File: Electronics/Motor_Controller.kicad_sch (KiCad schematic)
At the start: 4 parts, among them U1 RP2040, U4 W25Q32JVZP

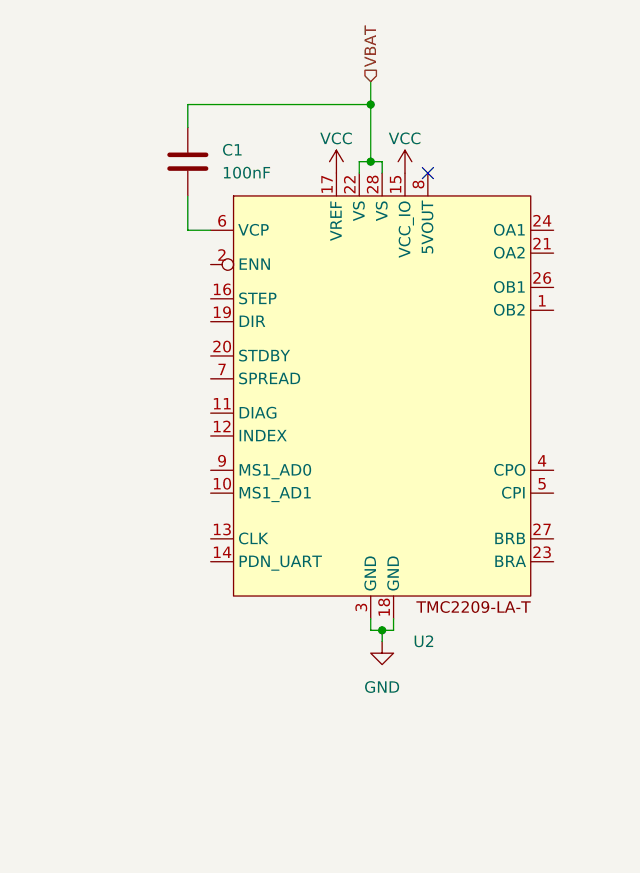
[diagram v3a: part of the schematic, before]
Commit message: update gitignore
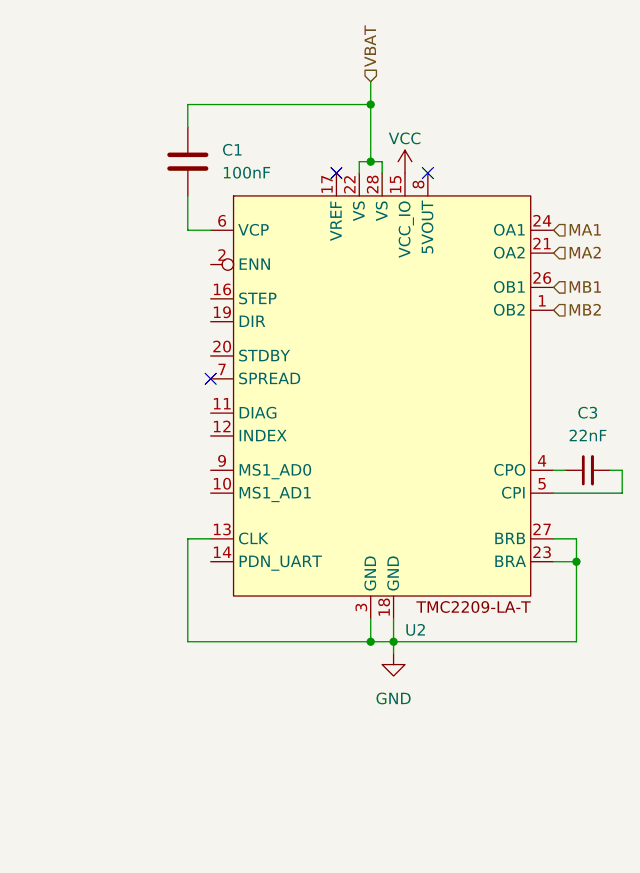
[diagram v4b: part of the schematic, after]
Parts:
- added C3: 22nF, symbol Device:C_Small
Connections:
- net GND: now also U2.13 (CLK), U2.23 (BRA), U2.27 (BRB)
- net VCC: no longer U2.17 (VREF)
- net MB2: now reaches U2.1 (OB2)
- net MA2: now reaches U2.21 (OA2)
- net MA1: now reaches U2.24 (OA1)
- net MB1: now reaches U2.26 (OB1)
- net at U2.4 (CPO): now also C3.1
- net at U2.5 (CPI): now also C3.2
- no-connect marks 1 -> 3
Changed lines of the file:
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@@
 (kicad_sch (version 20230121) (generator eeschema)
   (paper "A4")
+  (junction (at 196.85 87.63) (diameter 0) (color 0 0 0 0)
+  )
+  (junction (at 217.17 78.74) (diameter 0) (color 0 0 0 0)
+  )
   (junction (at 194.31 27.94) (diameter 0) (color 0 0 0 0)
   )
   (junction (at 194.31 34.29) (diameter 0) (color 0 0 0 0)
   )
-  (junction (at 195.58 86.36) (diameter 0) (color 0 0 0 0)
-  )
+  (junction (at 194.31 87.63) (diameter 0) (color 0 0 0 0)
+  )
+  (no_connect (at 190.5 35.56))
+  (no_connect (at 176.53 58.42))
   (no_connect (at 200.66 35.56))
   (wire (pts (xy 194.31 34.29) (xy 195.58 34.29))
     (stroke (width 0) (type default))
   )
+  (wire (pts (xy 214.63 68.58) (xy 215.9 68.58))
+    (stroke (width 0) (type default))
+  )
   (wire (pts (xy 194.31 25.4) (xy 194.31 27.94))
     (stroke (width 0) (type default))
   )
+  (wire (pts (xy 196.85 87.63) (xy 217.17 87.63))
+    (stroke (width 0) (type default))
+  )
   (wire (pts (xy 173.99 27.94) (xy 194.31 27.94))
     (stroke (width 0) (type default))
@@
     (stroke (width 0) (type default))
   )
-  (wire (pts (xy 194.31 85.09) (xy 194.31 86.36))
+  (wire (pts (xy 194.31 85.09) (xy 194.31 87.63))
+    (stroke (width 0) (type default))
+  )
+  (wire (pts (xy 222.25 71.12) (xy 214.63 71.12))
     (stroke (width 0) (type default))
   )
@@
     (stroke (width 0) (type default))
   )
+  (wire (pts (xy 217.17 87.63) (xy 217.17 78.74))
+    (stroke (width 0) (type default))
+  )
   (wire (pts (xy 173.99 41.91) (xy 173.99 38.1))
     (stroke (width 0) (type default))
   )
+  (wire (pts (xy 217.17 78.74) (xy 214.63 78.74))
+    (stroke (width 0) (type default))
+  )
   (wire (pts (xy 193.04 34.29) (xy 193.04 35.56))
     (stroke (width 0) (type default))
   )
+  (wire (pts (xy 217.17 76.2) (xy 217.17 78.74))
+    (stroke (width 0) (type default))
+  )
   (wire (pts (xy 194.31 27.94) (xy 194.31 34.29))
     (stroke (width 0) (type default))
   )
-  (wire (pts (xy 194.31 86.36) (xy 195.58 86.36))
-    (stroke (width 0) (type default))
-  )
-  (wire (pts (xy 195.58 86.36) (xy 196.85 86.36))
-    (stroke (width 0) (type default))
-  )
-  (wire (pts (xy 195.58 86.36) (xy 195.58 87.63))
-    (stroke (width 0) (type default))
-  )
-  (wire (pts (xy 196.85 85.09) (xy 196.85 86.36))
-    (stroke (width 0) (type default))
+  (wire (pts (xy 194.31 87.63) (xy 196.85 87.63))
+    (stroke (width 0) (type default))
+  )
+  (wire (pts (xy 173.99 87.63) (xy 194.31 87.63))
+    (stroke (width 0) (type default))
+  )
+  (wire (pts (xy 214.63 76.2) (xy 217.17 76.2))
+    (stroke (width 0) (type default))
+  )
+  (wire (pts (xy 173.99 76.2) (xy 173.99 87.63))
+    (stroke (width 0) (type default))
+  )
+  (wire (pts (xy 196.85 88.9) (xy 196.85 87.63))
+    (stroke (width 0) (type default))
+  )
+  (wire (pts (xy 222.25 68.58) (xy 222.25 71.12))
+    (stroke (width 0) (type default))
+  )
+  (wire (pts (xy 196.85 85.09) (xy 196.85 87.63))
+    (stroke (width 0) (type default))
+  )
+  (wire (pts (xy 176.53 76.2) (xy 173.99 76.2))
+    (stroke (width 0) (type default))
+  )
+  (wire (pts (xy 220.98 68.58) (xy 222.25 68.58))
+    (stroke (width 0) (type default))
+  )
+  (hierarchical_label "MB2" (shape input) (at 214.63 50.8 0) (fields_autoplaced)
+    (effects (font (size 1.27 1.27)) (justify left))
+  )
+  (hierarchical_label "MA2" (shape input) (at 214.63 44.45 0) (fields_autoplaced)
+    (effects (font (size 1.27 1.27)) (justify left))
+  )
+  (hierarchical_label "MA1" (shape input) (at 214.63 41.91 0) (fields_autoplaced)
+    (effects (font (size 1.27 1.27)) (justify left))
   )
   (hierarchical_label "VBAT" (shape input) (at 194.31 25.4 90) (fields_autoplaced)
     (effects (font (size 1.27 1.27)) (justify left))
   )
+  (hierarchical_label "MB1" (shape input) (at 214.63 48.26 0) (fields_autoplaced)
+    (effects (font (size 1.27 1.27)) (justify left))
+  )
   (symbol (lib_id "TMC2209-LA-T:TMC2209-LA-T") (at 195.58 60.96 0) (unit 1)
-    (in_bom yes) (on_board yes) (dnp no) (fields_autoplaced)
-    (property "Reference" "U2" (at 199.0441 87.63 0)
+    (in_bom yes) (on_board yes) (dnp no)
+    (property "Reference" "U2" (at 198.12 86.36 0)
       (effects (font (size 1.27 1.27)) (justify left))
     )
@@
         (path "/4c70cac4-2e87-4919-a1c8-fe5f41acf493/95aef9fc-3811-4af8-99a5-cda59dbef7fc"
           (reference "U2") (unit 1)
-        )
-      )
-    )
-  )
-  (symbol (lib_id "power:VCC") (at 190.5 35.56 0) (unit 1)
-    (in_bom yes) (on_board yes) (dnp no)
-    (property "Reference" "#PWR06" (at 190.5 39.37 0)
-      (effects (font (size 1.27 1.27)) hide)
-    )
-    (property "Value" "VCC" (at 190.5 31.75 0)
-      (effects (font (size 1.27 1.27)))
-    )
-    (property "Footprint" "" (at 190.5 35.56 0)
-      (effects (font (size 1.27 1.27)) hide)
-    )
-    (property "Datasheet" "" (at 190.5 35.56 0)
-      (effects (font (size 1.27 1.27)) hide)
-    )
-    (pin "1")
-    (instances
-      (project "Electronics"
-        (path "/4c70cac4-2e87-4919-a1c8-fe5f41acf493/95aef9fc-3811-4af8-99a5-cda59dbef7fc"
-          (reference "#PWR06") (unit 1)
         )
       )
@@
     )
   )
+  (symbol (lib_id "Device:C_Small") (at 218.44 68.58 90) (unit 1)
+    (in_bom yes) (on_board yes) (dnp no)
+    (property "Reference" "C3" (at 218.4463 62.23 90)
+      (effects (font (size 1.27 1.27)))
+    )
+    (property "Value" "22nF" (at 218.44 64.77 90)
+      (effects (font (size 1.27 1.27)))
+    )
+    (property "Footprint" "" (at 218.44 68.58 0)
+      (effects (font (size 1.27 1.27)) hide)
+    )
+    (property "Datasheet" "~" (at 218.44 68.58 0)
+      (effects (font (size 1.27 1.27)) hide)
+    )
+    (pin "1")
+    (pin "2")
+    (instances
+      (project "Electronics"
+        (path "/4c70cac4-2e87-4919-a1c8-fe5f41acf493/95aef9fc-3811-4af8-99a5-cda59dbef7fc"
+          (reference "C3") (unit 1)
+        )
+      )
+    )
+  )
   (symbol (lib_id "Device:C") (at 173.99 34.29 0) (unit 1)
     (in_bom yes) (on_board yes) (dnp no)
@@
     )
   )
-  (symbol (lib_id "power:GND") (at 195.58 87.63 0) (unit 1)
+  (symbol (lib_id "power:GND") (at 196.85 88.9 0) (unit 1)
     (in_bom yes) (on_board yes) (dnp no) (fields_autoplaced)
-    (property "Reference" "#PWR08" (at 195.58 93.98 0)
-      (effects (font (size 1.27 1.27)) hide)
-    )
-    (property "Value" "GND" (at 195.58 92.71 0)
-      (effects (font (size 1.27 1.27)))
-    )
-    (property "Footprint" "" (at 195.58 87.63 0)
-      (effects (font (size 1.27 1.27)) hide)
-    )
-    (property "Datasheet" "" (at 195.58 87.63 0)
-      (effects (font (size 1.27 1.27)) hide)
-    )
+    (property "Reference" "#PWR08" (at 196.85 95.25 0)
+      (effects (font (size 1.27 1.27)) hide)
+    )
+    (property "Value" "GND" (at 196.85 93.98 0)
+      (effects (font (size 1.27 1.27)))
+    )
+    (property "Footprint" "" (at 196.85 88.9 0)
+      (effects (font (size 1.27 1.27)) hide)
+    )
+    (property "Datasheet" "" (at 196.85 88.9 0)
+      (effects (font (size 1.27 1.27)) hide)
+    )

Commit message: motor driver finished!
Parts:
- added C10, C11, C12, C13, C14, C17, C18, C22, C5, C7, C8, C9: 100nF, symbol Device:C
- added C15, C16, C4: 1uF, symbol Device:C
- added C19, C20: 15pF, symbol Device:C
- added C21: 10uF, symbol Device:C
- added C6: 22nF, symbol Device:C_Small
- added D2: ML_LED, symbol Device:LED
- added D3: MR_LED, symbol Device:LED
- added D4: RP2040_LED, symbol Device:LED
- added J2: SWCLK SWD, symbol Connector:Conn_01x02_Pin
- added R10, R9: 27.4, symbol Device:R
- added R11, R12, R4, R5, R6, R7, R8: 1k, symbol Device:R
- added R2: 22k, symbol Device:R
- added R3: 10k, symbol Device:R
- added SW1: SW_Push, symbol Switch:SW_Push
- added SW2: ~{USB_BOOT}, symbol Switch:SW_SPST
- added U6: ~, Package_DFN_QFN:QFN-28-1EP_5x5mm_P0.5mm_EP3.75x3.75mm, symbol TMC2209-LA-T:TMC2209-LA-T
- added Y1: ABM8-272-T3, symbol Device:Crystal_GND24
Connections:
- net GND: now also U1.19 (TESTEN), U1.57 (GND), U2.20 (STDBY), U4.4 (GND), U4.9 (EP), C10.2, C11.2, C12.2, C13.2, C14.2, C15.2, C16.2, C17.2, C18.2, C19.1, C20.1, C21.2, C22.2, C4.2, C7.2, C8.2, C9.2, D2.1 (K), D3.1 (K), D4.1 (K), SW1.1, SW2.2 (B), U6.13 (CLK), U6.18 (GND), U6.20 (STDBY), U6.23 (BRA), U6.27 (BRB), U6.3 (GND), Y1.2, Y1.4
- net VBAT: now also C5.1, U6.22 (VS), U6.28 (VS)
- net VCC: now also U1.1 (IOVDD), U1.10 (IOVDD), U1.22 (IOVDD), U1.33 (IOVDD), U1.42 (IOVDD), U1.43 (ADC_AVDD), U1.44 (VREG_IN), U1.48 (USB_VDD), U1.49 (IOVDD), U4.8 (VCC), C10.1, C11.1, C12.1, C13.1, C14.1, C15.1, C21.1, C7.1, C8.1, C9.1, R11.1, R3.1, U6.15 (VCC_IO)
- net ML_DIAG: now reaches U2.11 (DIAG)
- net ML_DIAG: now also U1.16 (GPIO13)
- net ML_INDEX: now reaches U2.12 (INDEX)
- net ML_INDEX: now also U1.17 (GPIO14)
- net ML_UART: now reaches U2.14 (PDN_UART)
- net ML_UART: now also U1.3 (GPIO1), R6.2
- net ML_STEP: now reaches U2.16 (STEP)
- net ML_STEP: now also U1.13 (GPIO10)
- net CURR_S: now reaches U2.17 (VREF)
- net CURR_S: now also U1.11 (GPIO8), C4.1, R2.2, U6.17 (VREF)
- net ML_DIR: now reaches U2.19 (DIR)
- net ML_DIR: now also U1.14 (GPIO11)
- net ~{ML_EN}: now reaches U2.2 (ENN)
- net ~{ML_EN}: now also U1.12 (GPIO9)
- net ML_SPRD: now reaches U2.7 (SPREAD)
- net ML_SPRD: now also U1.15 (GPIO12)
- net at U2.8 (5VOUT): now also R4.1
- net ~{MR_EN}: now reaches U1.18 (GPIO15)
- net ~{MR_EN}: now also U6.2 (ENN)
- net at U1.2 (GPIO0): now also R6.1
- net at U1.20 (XIN): now also C19.2, Y1.1
- net at U1.21 (XOUT): now also C20.2, Y1.3
- net at U1.23 (DVDD), U1.50 (DVDD): now also U1.45 (VREG_VOUT), C16.1, C17.1, C18.1
- net at U1.24 (SWCLK): now also J2.1 (Pin_1)
- net at U1.25 (SWD): now also J2.2 (Pin_2)
- net at U1.26 (RUN): now also C22.1, R11.2, SW1.2
- net MR_STEP: now reaches U1.27 (GPIO16)
- net MR_STEP: now also U6.16 (STEP)
- net MR_DIR: now reaches U1.28 (GPIO17)
- net MR_DIR: now also U6.19 (DIR)
- net MR_SPRD: now reaches U1.29 (GPIO18)
- net MR_SPRD: now also U6.7 (SPREAD)
- net MR_DIAG: now reaches U1.30 (GPIO19)
- net MR_DIAG: now also U6.11 (DIAG)
- net MR_INDEX: now reaches U1.31 (GPIO20)
- net MR_INDEX: now also U6.12 (INDEX)
- net at U1.32 (GPIO21): now also R8.1
- net SDA: now reaches U1.34 (GPIO22)
- net SCL: now reaches U1.35 (GPIO23)
- net at U1.37 (GPIO25): now also R2.1
- net at U1.46 (USB_DM): now also R10.2
- net at U1.47 (USB_DP): now also R9.2
- net QSPI_SD3: now reaches U1.51 (QSPI_SD3)
- net QSPI_SD3: now also U4.7 (IO3)
- net QSPI_SCLK: now reaches U1.52 (QSPI_SCLK)
- net QSPI_SCLK: now also U4.6 (CLK)
- net QSPI_SD0: now reaches U1.53 (QSPI_SD0)
- net QSPI_SD0: now also U4.5 (DI(IO0))
- net QSPI_SD2: now reaches U1.54 (QSPI_SD2)
- net QSPI_SD2: now also U4.3 (IO2)
- net QSPI_SD1: now reaches U1.55 (QSPI_SD1)
- net QSPI_SD1: now also U4.2 (DO(IO1))
- net QSPI_SS: now reaches U1.56 (QSPI_SS)
- net QSPI_SS: now also U4.1 (~{CS}), R12.1, R3.2
- net at U1.6 (GPIO4): now also R7.1
- net MR_UART: now reaches U1.7 (GPIO5)
- net MR_UART: now also R7.2, U6.14 (PDN_UART)
- net MA1 renamed ML_A1
- net MA2 renamed ML_A2
- net MB1 renamed ML_B1
- net MB2 renamed ML_B2
- new net: C6.1, U6.4 (CPO)
- new net: C6.2, U6.5 (CPI)
- new net: C5.2, U6.6 (VCP)
- new net: R5.1, U6.8 (5VOUT)
- new net: R12.2, SW2.1 (A)
- new net: D2.2 (A), R4.2
- new net: D3.2 (A), R5.2
- new net: D4.2 (A), R8.2
- new net MR_A1: U6.24 (OA1)
- new net MR_A2: U6.21 (OA2)
- new net MR_B1: U6.26 (OB1)
- new net MR_B2: U6.1 (OB2)
- new net USB+: R9.1
- new net USB-: R10.1
- no-connect marks 3 -> 13
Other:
- note added: "FLASH MEMORY"
- note added: "MCU"
- note added: "MOTOR DRIVERS"
- note added: "POWER"
- moved on the sheet: C1, C3, U1, U2, U4

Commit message: gyros done
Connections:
- net READY: now reaches U1.36 (GPIO24)
- no-connect marks 13 -> 12
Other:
- moved on the sheet: C4, R2
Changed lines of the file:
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@@
   (junction (at 160.02 121.92) (diameter 0) (color 0 0 0 0)
   )
-  (junction (at 118.11 105.41) (diameter 0) (color 0 0 0 0)
+  (junction (at 121.92 105.41) (diameter 0) (color 0 0 0 0)
   )
   (junction (at 182.88 121.92) (diameter 0) (color 0 0 0 0)
@@
   (junction (at 203.2 86.36) (diameter 0) (color 0 0 0 0)
   )
+  (junction (at 121.92 128.27) (diameter 0) (color 0 0 0 0)
+  )
   (junction (at 38.1 87.63) (diameter 0) (color 0 0 0 0)
   )
@@
   )
   (junction (at 44.45 179.07) (diameter 0) (color 0 0 0 0)
-  )
-  (junction (at 118.11 128.27) (diameter 0) (color 0 0 0 0)
   )
   (junction (at 19.05 97.79) (diameter 0) (color 0 0 0 0)
@@
   (no_connect (at 162.56 67.31))
   (no_connect (at 106.68 115.57))
-  (no_connect (at 106.68 102.87))
   (no_connect (at 106.68 59.69))
   (no_connect (at 229.87 69.85))
@@
     (stroke (width 0) (type default))
   )
-  (wire (pts (xy 116.84 105.41) (xy 118.11 105.41))
+  (wire (pts (xy 120.65 105.41) (xy 121.92 105.41))
     (stroke (width 0) (type default))
   )
@@
     (stroke (width 0) (type default))
   )
-  (wire (pts (xy 118.11 105.41) (xy 118.11 109.22))
-    (stroke (width 0) (type default))
-  )
-  (wire (pts (xy 118.11 128.27) (xy 134.62 128.27))
+  (wire (pts (xy 121.92 105.41) (xy 121.92 109.22))
     (stroke (width 0) (type default))
   )
@@
     (stroke (width 0) (type default))
   )
-  (wire (pts (xy 118.11 128.27) (xy 118.11 116.84))
+  (wire (pts (xy 121.92 128.27) (xy 121.92 116.84))
     (stroke (width 0) (type default))
   )
@@
     (stroke (width 0) (type default))
   )
-  (wire (pts (xy 81.28 128.27) (xy 118.11 128.27))
+  (wire (pts (xy 81.28 128.27) (xy 121.92 128.27))
     (stroke (width 0) (type default))
   )
@@
     (stroke (width 0) (type default))
   )
-  (wire (pts (xy 106.68 105.41) (xy 109.22 105.41))
+  (wire (pts (xy 106.68 105.41) (xy 113.03 105.41))
     (stroke (width 0) (type default))
   )
@@
     (stroke (width 0) (type default))
   )
+  (wire (pts (xy 121.92 128.27) (xy 134.62 128.27))
+    (stroke (width 0) (type default))
+  )
   (wire (pts (xy 119.38 22.86) (xy 119.38 24.13))
     (stroke (width 0) (type default))
@@
     (stroke (width 0) (type default))
   )
-  (wire (pts (xy 118.11 105.41) (xy 127 105.41))
+  (wire (pts (xy 121.92 105.41) (xy 130.81 105.41))
     (stroke (width 0) (type default))
   )
@@
     (effects (font (size 1.27 1.27)) (justify right bottom))
   )
-  (label "CURR_S" (at 127 105.41 180) (fields_autoplaced)
+  (label "CURR_S" (at 130.81 105.41 180) (fields_autoplaced)
     (effects (font (size 1.27 1.27)) (justify right bottom))
   )
@@
   )
   (hierarchical_label "MR_B1" (shape output) (at 267.97 46.99 0) (fields_autoplaced)
+    (effects (font (size 1.27 1.27)) (justify left))
+  )
+  (hierarchical_label "READY" (shape output) (at 106.68 102.87 0) (fields_autoplaced)
     (effects (font (size 1.27 1.27)) (justify left))
   )
@@
     )
   )
-  (symbol (lib_id "Device:R") (at 113.03 105.41 90) (unit 1)
-    (in_bom yes) (on_board yes) (dnp no)
-    (property "Reference" "R2" (at 113.03 102.87 90)
-      (effects (font (size 1.27 1.27)))
-    )
-    (property "Value" "22k" (at 113.03 105.41 90)
-      (effects (font (size 1.27 1.27)))
-    )
-    (property "Footprint" "" (at 113.03 107.188 90)
-      (effects (font (size 1.27 1.27)) hide)
-    )
-    (property "Datasheet" "~" (at 113.03 105.41 0)
+  (symbol (lib_id "Device:R") (at 116.84 105.41 90) (unit 1)
+    (in_bom yes) (on_board yes) (dnp no)
+    (property "Reference" "R2" (at 116.84 102.87 90)
+      (effects (font (size 1.27 1.27)))
+    )
+    (property "Value" "22k" (at 116.84 105.41 90)
+      (effects (font (size 1.27 1.27)))
+    )
+    (property "Footprint" "" (at 116.84 107.188 90)
+      (effects (font (size 1.27 1.27)) hide)
+    )
+    (property "Datasheet" "~" (at 116.84 105.41 0)
       (effects (font (size 1.27 1.27)) hide)
     )
@@
     )
   )
-  (symbol (lib_id "Device:C") (at 118.11 113.03 0) (unit 1)
-    (in_bom yes) (on_board yes) (dnp no)
-    (property "Reference" "C4" (at 121.92 111.76 0)
-      (effects (font (size 1.27 1.27)) (justify left))
-    )
-    (property "Value" "1uF" (at 121.92 114.3 0)
-      (effects (font (size 1.27 1.27)) (justify left))
-    )
-    (property "Footprint" "" (at 119.0752 116.84 0)
-      (effects (font (size 1.27 1.27)) hide)
-    )
-    (property "Datasheet" "~" (at 118.11 113.03 0)
-      (effects (font (size 1.27 1.27)) hide)
-    )
+  (symbol (lib_id "Device:C") (at 121.92 113.03 0) (unit 1)
+    (in_bom yes) (on_board yes) (dnp no)
+    (property "Reference" "C4" (at 125.73 111.76 0)
+      (effects (font (size 1.27 1.27)) (justify left))
+    )
+    (property "Value" "1uF" (at 125.73 114.3 0)
+      (effects (font (size 1.27 1.27)) (justify left))
+    )
+    (property "Footprint" "" (at 122.8852 116.84 0)
+      (effects (font (size 1.27 1.27)) hide)
+    )
+    (property "Datasheet" "~" (at 121.92 113.03 0)
+      (effects (font (size 1.27 1.27)) hide)
+    )
